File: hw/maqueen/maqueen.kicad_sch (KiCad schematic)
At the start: 29 parts, among them IC1 MSP430FR2355TPT, J1 conn_DFrobot, J2 ESP01, J3 SBW, SW1 RST, U1 LMV324, Y1 Crystal

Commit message: testing points & minor adjustements
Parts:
- added TP1: RST_TDO/TDI, Connector_PinHeader_1.00mm:PinHeader_1x01_P1.00mm_Vertical, symbol Connector:TestPoint
- added TP10: ACLK, Connector_PinHeader_1.00mm:PinHeader_1x01_P1.00mm_Vertical, symbol Connector:TestPoint
- added TP2: uC_VCC, Connector_PinHeader_1.00mm:PinHeader_1x01_P1.00mm_Vertical, symbol Connector:TestPoint
- added TP3: SDA_I2C, Connector_PinHeader_1.00mm:PinHeader_1x01_P1.00mm_Vertical, symbol Connector:TestPoint
- added TP4: SCL_I2C, Connector_PinHeader_1.00mm:PinHeader_1x01_P1.00mm_Vertical, symbol Connector:TestPoint
- added TP5: UART_RX, Connector_PinHeader_1.00mm:PinHeader_1x01_P1.00mm_Vertical, symbol Connector:TestPoint
- added TP6: UART_TX, Connector_PinHeader_1.00mm:PinHeader_1x01_P1.00mm_Vertical, symbol Connector:TestPoint
- added TP7: LDR2, Connector_PinHeader_1.00mm:PinHeader_1x01_P1.00mm_Vertical, symbol Connector:TestPoint
- added TP8: LDR1, Connector_PinHeader_1.00mm:PinHeader_1x01_P1.00mm_Vertical, symbol Connector:TestPoint
- added TP9: SMCLK, Connector_PinHeader_1.00mm:PinHeader_1x01_P1.00mm_Vertical, symbol Connector:TestPoint
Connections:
- net +3.3V: now also TP2.1
- net FB_JOYSTICK: now also TP10.1
- net PHOTO1: now also TP8.1
- net PHOTO2: now also TP7.1, TP9.1
- net SCL_I2C: now also TP4.1
- net SDA_I2C: now also TP3.1
- net TDO/TDI: now also TP1.1
- net WIFI_UART_RX: now also TP5.1
- net WIFI_UART_TX: now also TP6.1
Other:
- moved on the sheet: R1, RV1

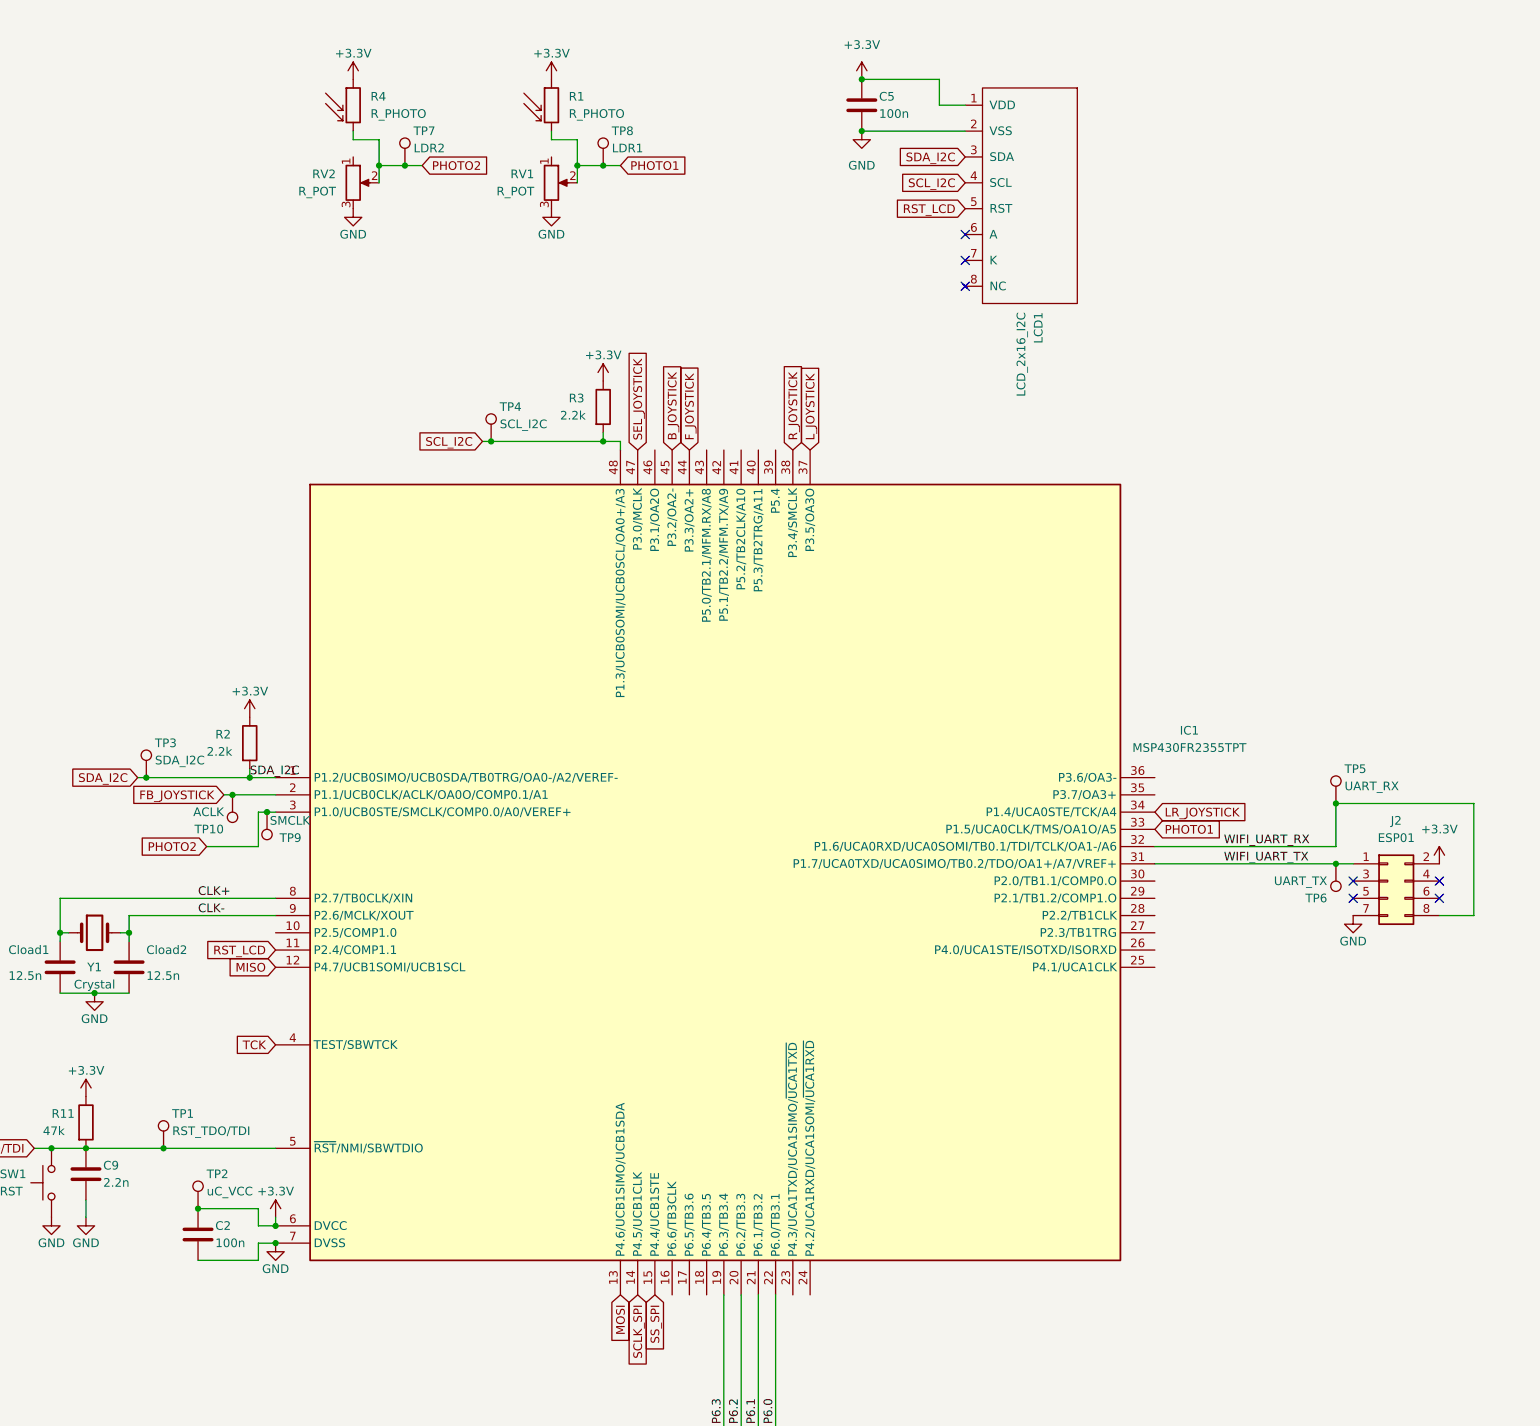
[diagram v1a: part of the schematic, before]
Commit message: tot drc be, menys huellas i serigrafia
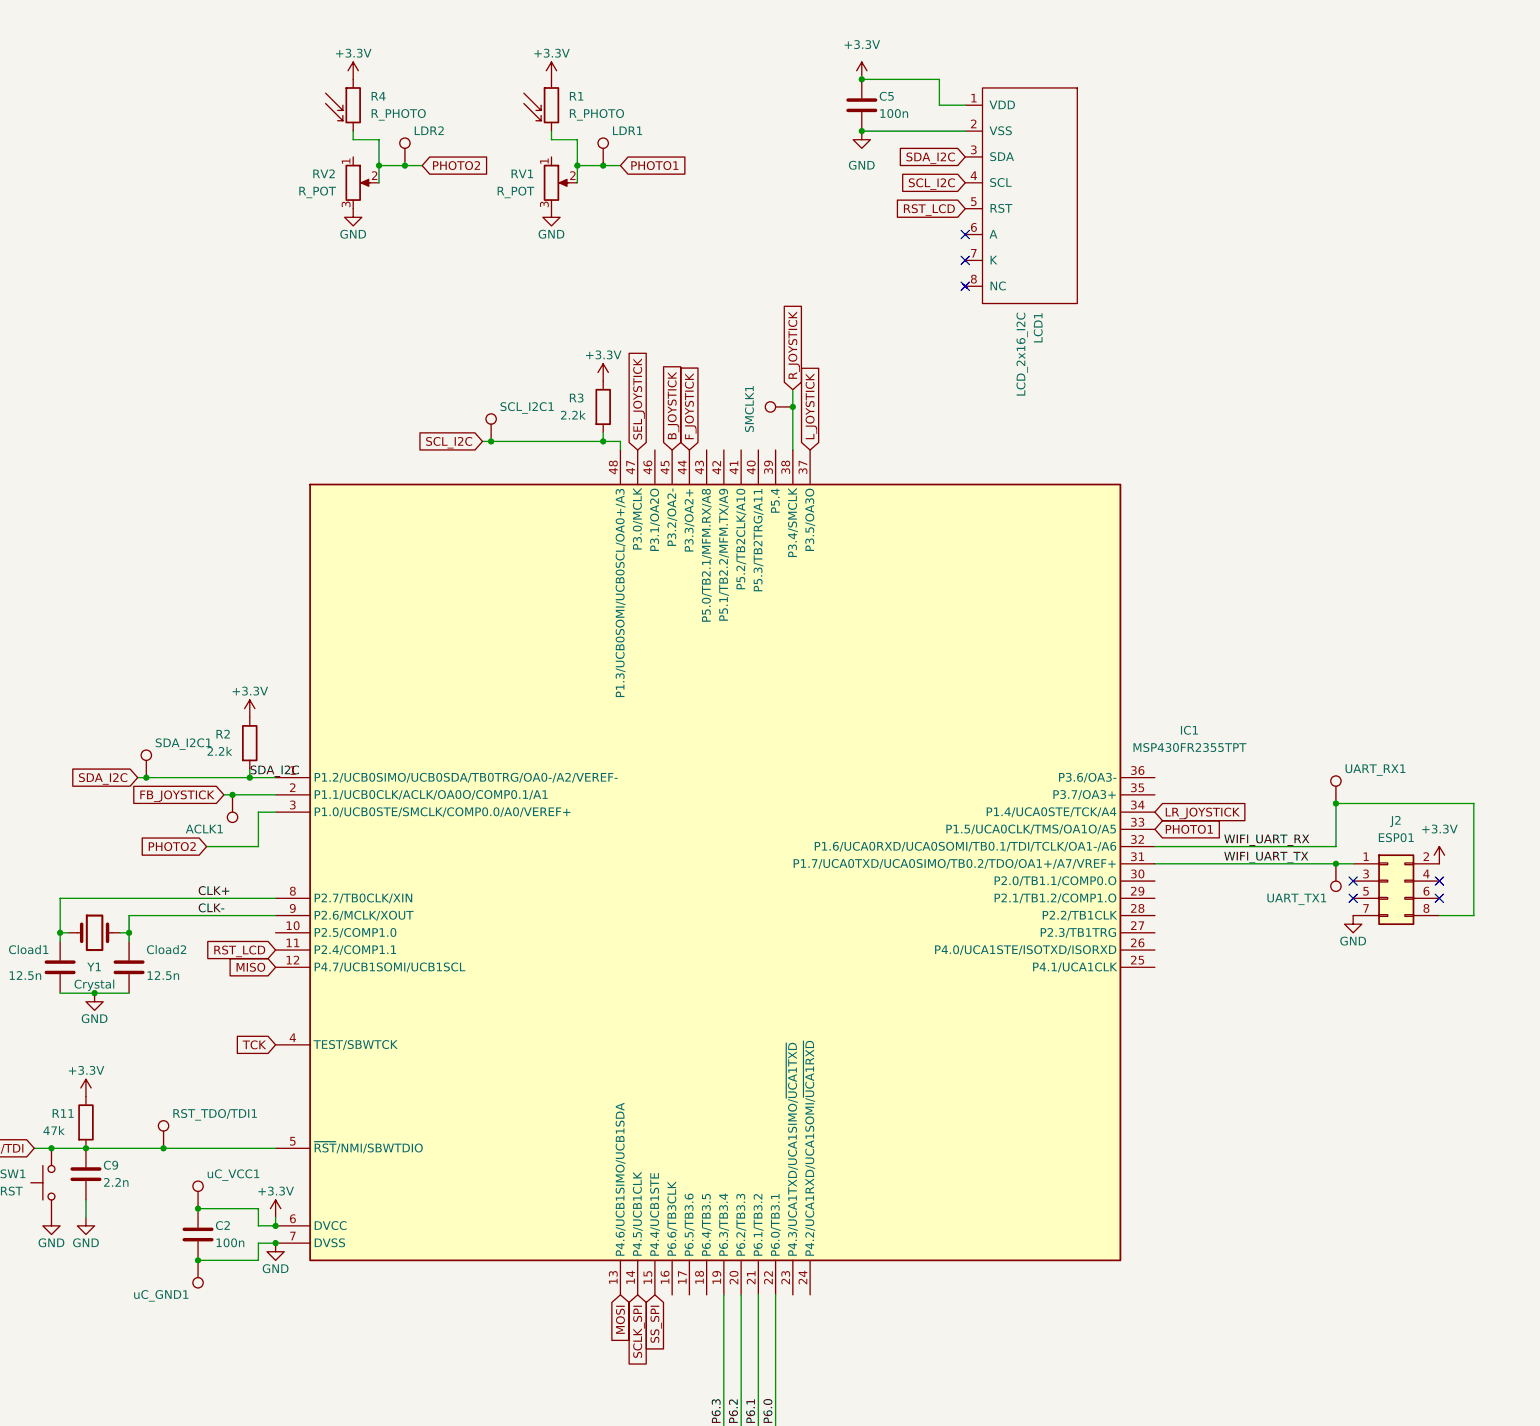
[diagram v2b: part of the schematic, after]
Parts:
- removed TP9: SMCLK, Connector_PinHeader_1.00mm:PinHeader_1x01_P1.00mm_Vertical, symbol Connector:TestPoint
- added SMCLK1, uC_GND1: ~, Connector_PinHeader_2.54mm:PinHeader_1x01_P2.54mm_Vertical, symbol Connector:TestPoint
- ACLK1: renamed from TP10; value ACLK -> ~; footprint Connector_PinHeader_1.00mm:PinHeader_1x01_P1.00mm_Vertical -> Connector_PinHeader_2.54mm:PinHeader_1x01_P2.54mm_Vertical
- LDR1: renamed from TP8; value LDR1 -> ~; footprint Connector_PinHeader_1.00mm:PinHeader_1x01_P1.00mm_Vertical -> Connector_PinHeader_2.54mm:PinHeader_1x01_P2.54mm_Vertical
- LDR2: renamed from TP7; value LDR2 -> ~; footprint Connector_PinHeader_1.00mm:PinHeader_1x01_P1.00mm_Vertical -> Connector_PinHeader_2.54mm:PinHeader_1x01_P2.54mm_Vertical
- RST_TDO/TDI1: renamed from TP1; value RST_TDO/TDI -> ~; footprint Connector_PinHeader_1.00mm:PinHeader_1x01_P1.00mm_Vertical -> Connector_PinHeader_2.54mm:PinHeader_1x01_P2.54mm_Vertical
- SCL_I2C1: renamed from TP4; value SCL_I2C -> ~; footprint Connector_PinHeader_1.00mm:PinHeader_1x01_P1.00mm_Vertical -> Connector_PinHeader_2.54mm:PinHeader_1x01_P2.54mm_Vertical
- SDA_I2C1: renamed from TP3; value SDA_I2C -> ~; footprint Connector_PinHeader_1.00mm:PinHeader_1x01_P1.00mm_Vertical -> Connector_PinHeader_2.54mm:PinHeader_1x01_P2.54mm_Vertical
- UART_RX1: renamed from TP5; value UART_RX -> ~; footprint Connector_PinHeader_1.00mm:PinHeader_1x01_P1.00mm_Vertical -> Connector_PinHeader_2.54mm:PinHeader_1x01_P2.54mm_Vertical
- UART_TX1: renamed from TP6; value UART_TX -> ~; footprint Connector_PinHeader_1.00mm:PinHeader_1x01_P1.00mm_Vertical -> Connector_PinHeader_2.54mm:PinHeader_1x01_P2.54mm_Vertical
- uC_VCC1: renamed from TP2; value uC_VCC -> ~; footprint Connector_PinHeader_1.00mm:PinHeader_1x01_P1.00mm_Vertical -> Connector_PinHeader_2.54mm:PinHeader_1x01_P2.54mm_Vertical
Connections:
- net GND: now also uC_GND1.1
- net R_JOYSTICK: now also SMCLK1.1

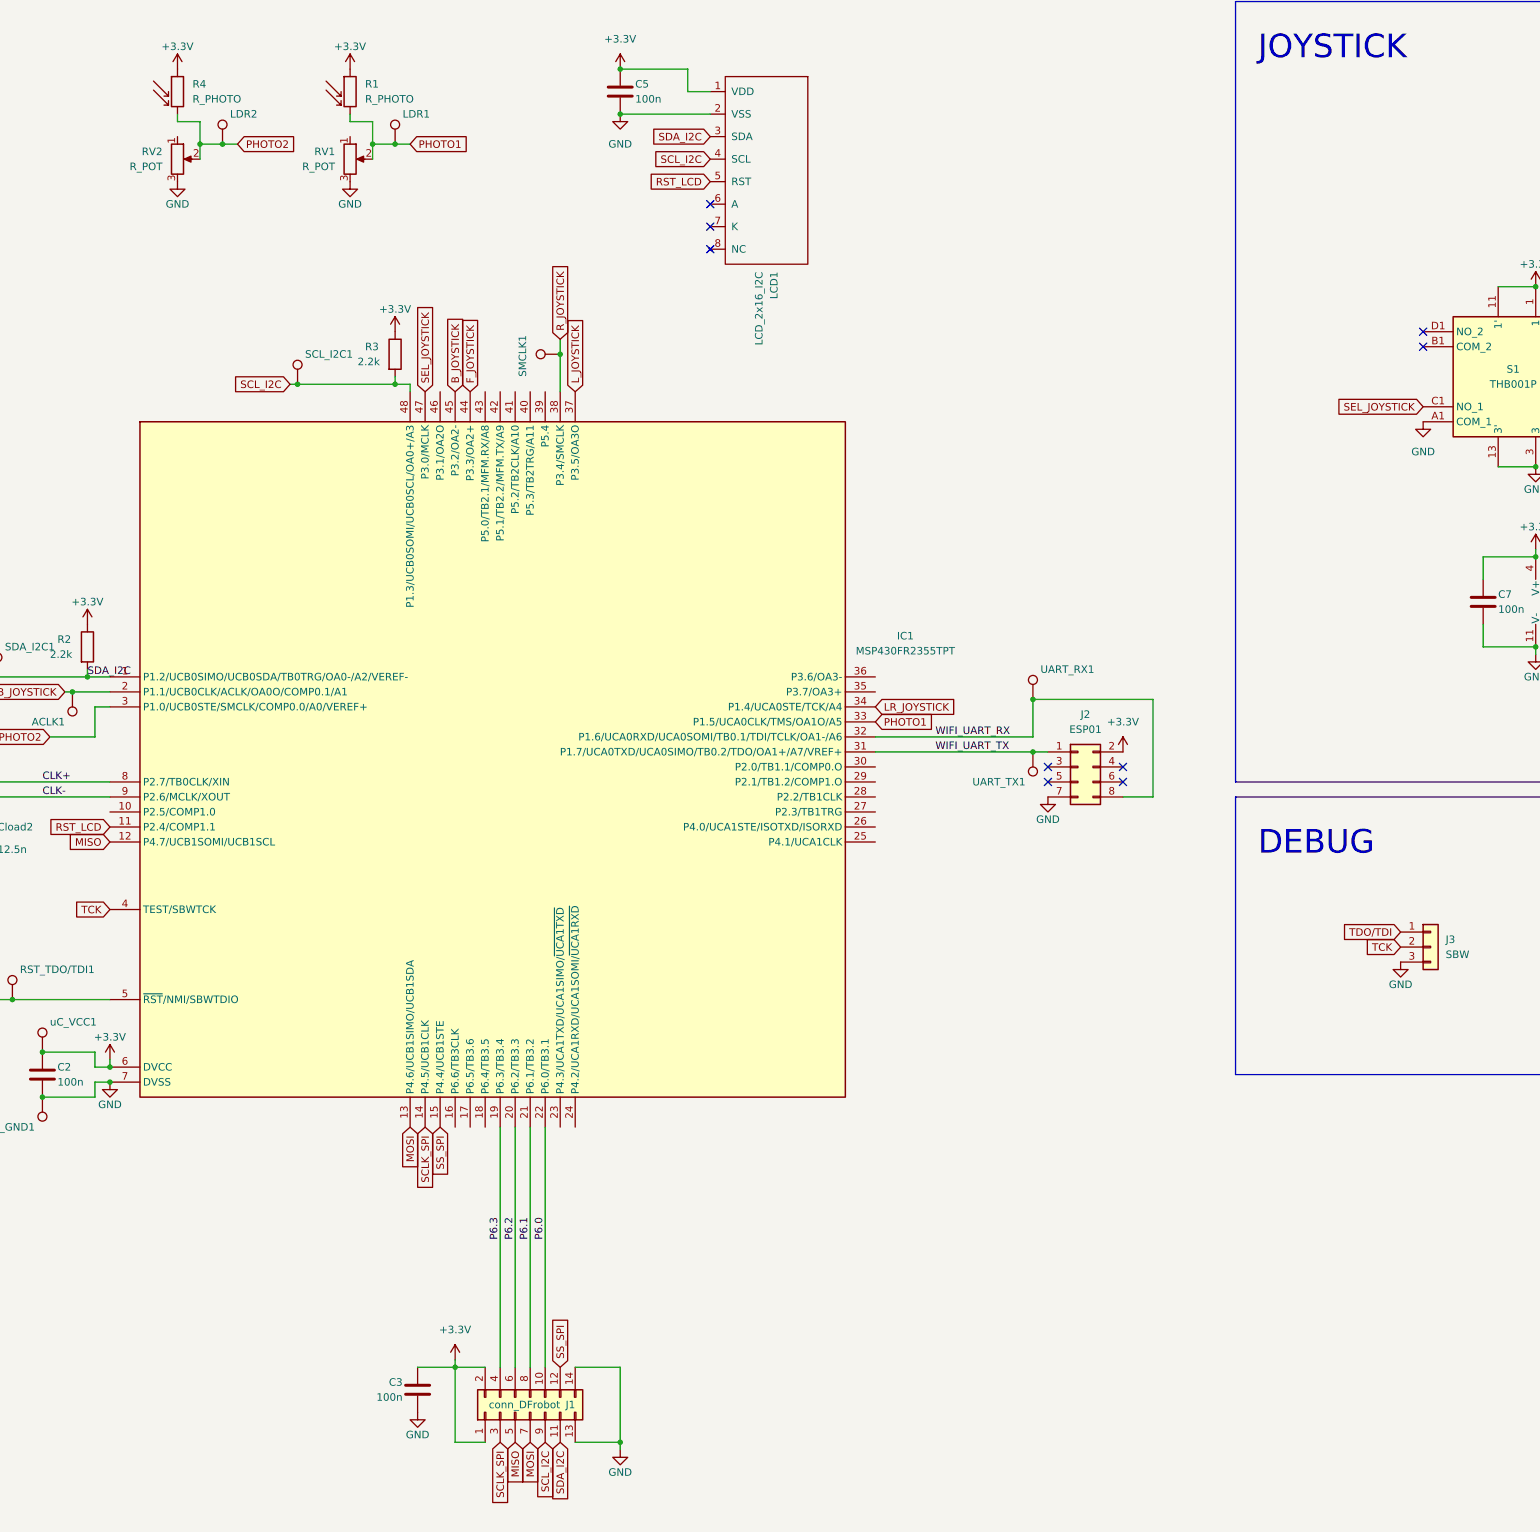
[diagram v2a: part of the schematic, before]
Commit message: afegit pullupR&debounceC a sel_joystick i noms a silkscreen
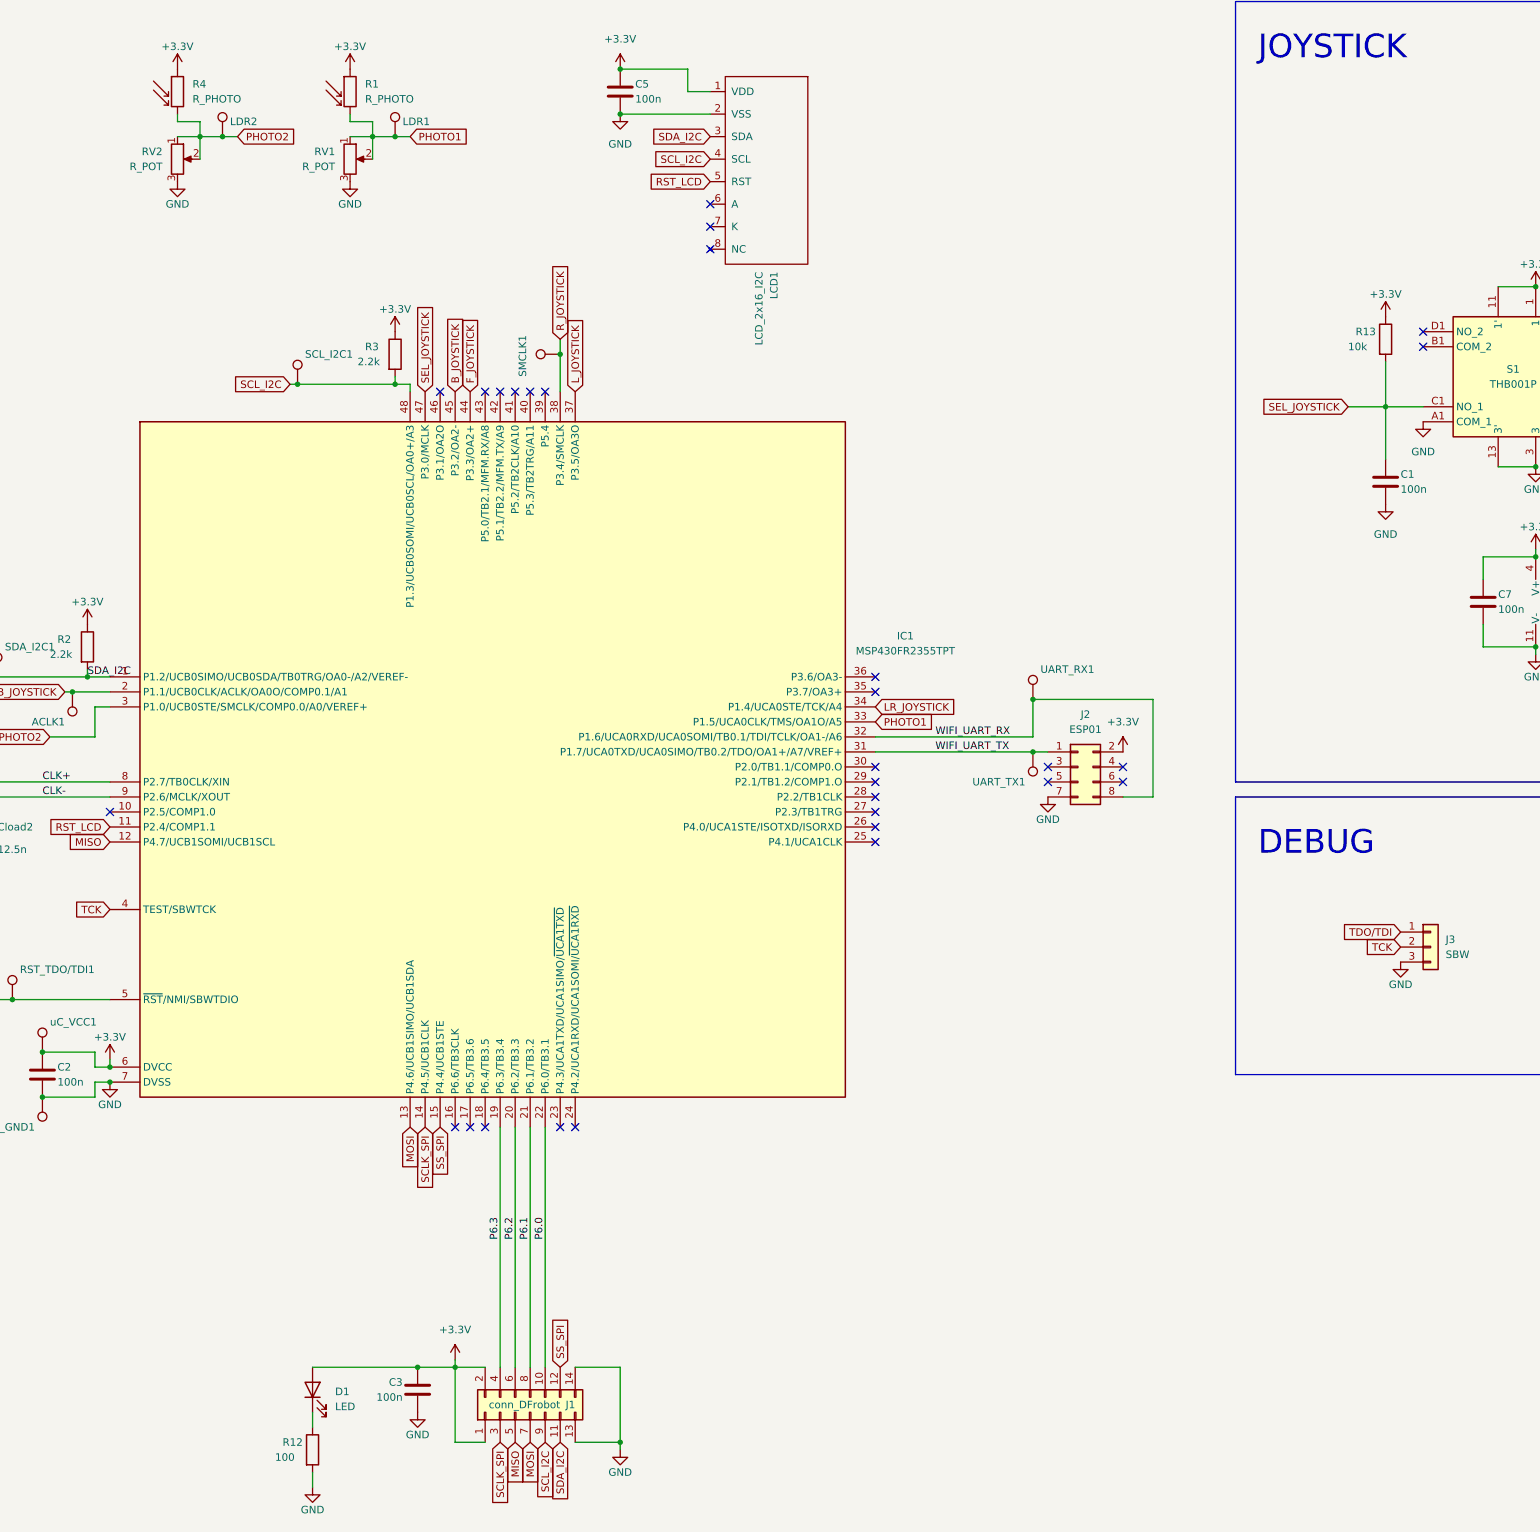
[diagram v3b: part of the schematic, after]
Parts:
- added C1: 100n, Capacitor_SMD:C_0805_2012Metric, symbol Device:C
- added D1: LED, symbol Device:LED
- added R12: 100, Resistor_SMD:R_0805_2012Metric, symbol Device:R
- added R13: 10k, Resistor_SMD:R_0805_2012Metric, symbol Device:R
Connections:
- net +3.3V: now also D1.2 (A), R13.1
- net GND: now also C1.2, R12.2
- net PHOTO1: now also RV1.1
- net PHOTO2: now also RV2.1
- net SEL_JOYSTICK: now also C1.1, R13.2
- new net: D1.1 (K), R12.1
- no-connect marks 9 -> 29
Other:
- title: (none) -> Disseny - MiSE
- moved on the sheet: LDR1, LDR2
